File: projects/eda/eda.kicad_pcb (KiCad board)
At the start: 2 copper layers, 24.5 x 54.5 mm, 5 parts

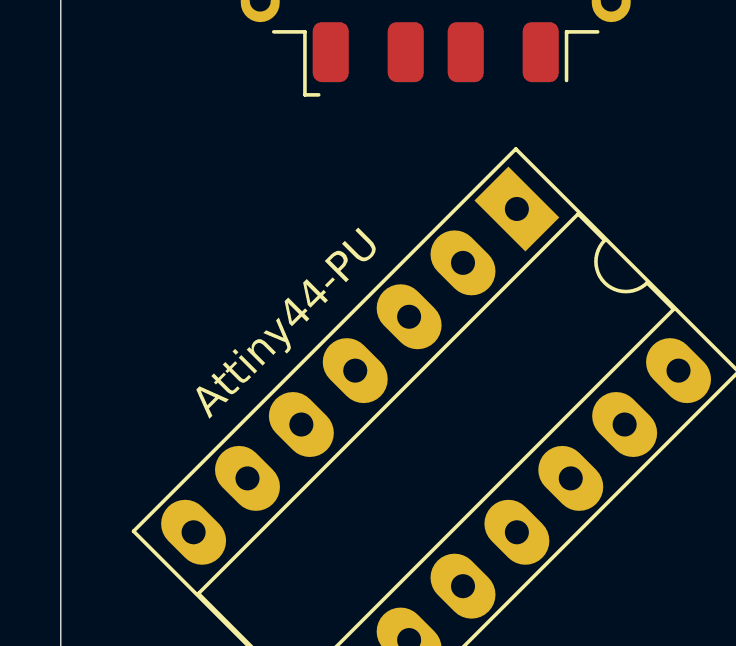
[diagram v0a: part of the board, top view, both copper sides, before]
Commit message: Add build scripts and update microcontroller. (#1)
* Port project to new microcontroller.

* Create make and build scripts.

* Update build script.

Updates the build script to use the new firmware target.

* Update PCB to reflect new microcontroller.
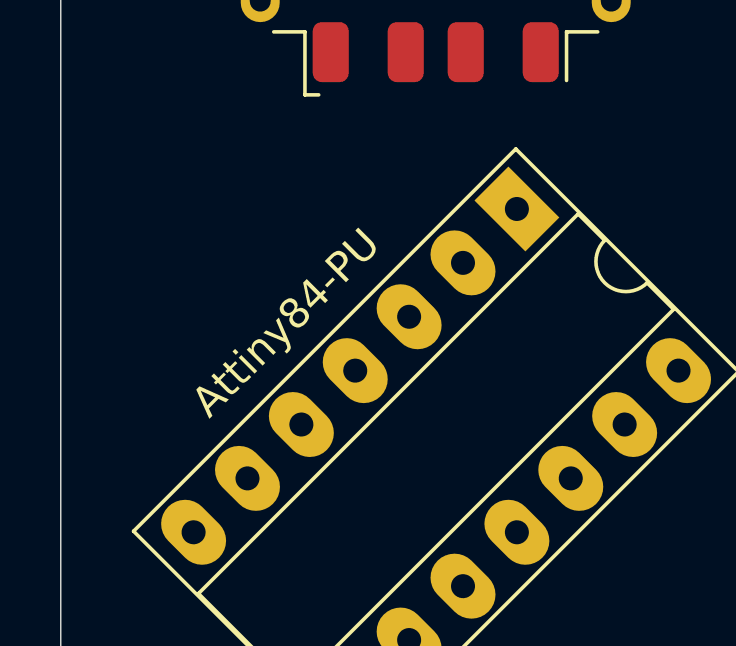
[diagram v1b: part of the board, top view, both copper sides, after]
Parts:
- renumbered Attiny44-PU to Attiny84-PU
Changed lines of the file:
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@@
 		(descr "14-lead though-hole mounted DIP package, row spacing 7.62 mm (300 mils), Socket, LongPads")
 		(tags "THT DIP DIL PDIP 2.54mm 7.62mm 300mil Socket LongPads")
-		(property "Reference" "Attiny44-PU"
-			(at -2.763821 8.132248 -135)
+		(property "Reference" "Attiny84-PU"
+			(at -2.763821 8.132248 225)
 			(layer "F.SilkS")
 			(effects
@@
 		(fp_arc
 			(start 4.810001 -1.33)
-			(mid 3.81 -0.33)
+			(mid 3.81 -0.330001)
 			(end 2.81 -1.33)
 			(stroke
@@
 		(tags "USB-A")
 		(property "Reference" "REF**"
-			(at 0 -7.5 270)
+			(at 0 -7.5 -90)
 			(layer "F.SilkS")
 			(hide yes)
@@
 		)
 		(property "Value" "USB_A_Molex_48037-2200_Horizontal"
-			(at 0 8 270)
+			(at 0 8 -90)
 			(layer "F.Fab")
 			(effects
@@
 		)
 		(fp_text user "${REFERENCE}"
-			(at 0 0 270)
-			(layer "F.Fab")
-			(effects
+			(at 0 0 -90)
+			(layer "F.Fab")
+			(effects

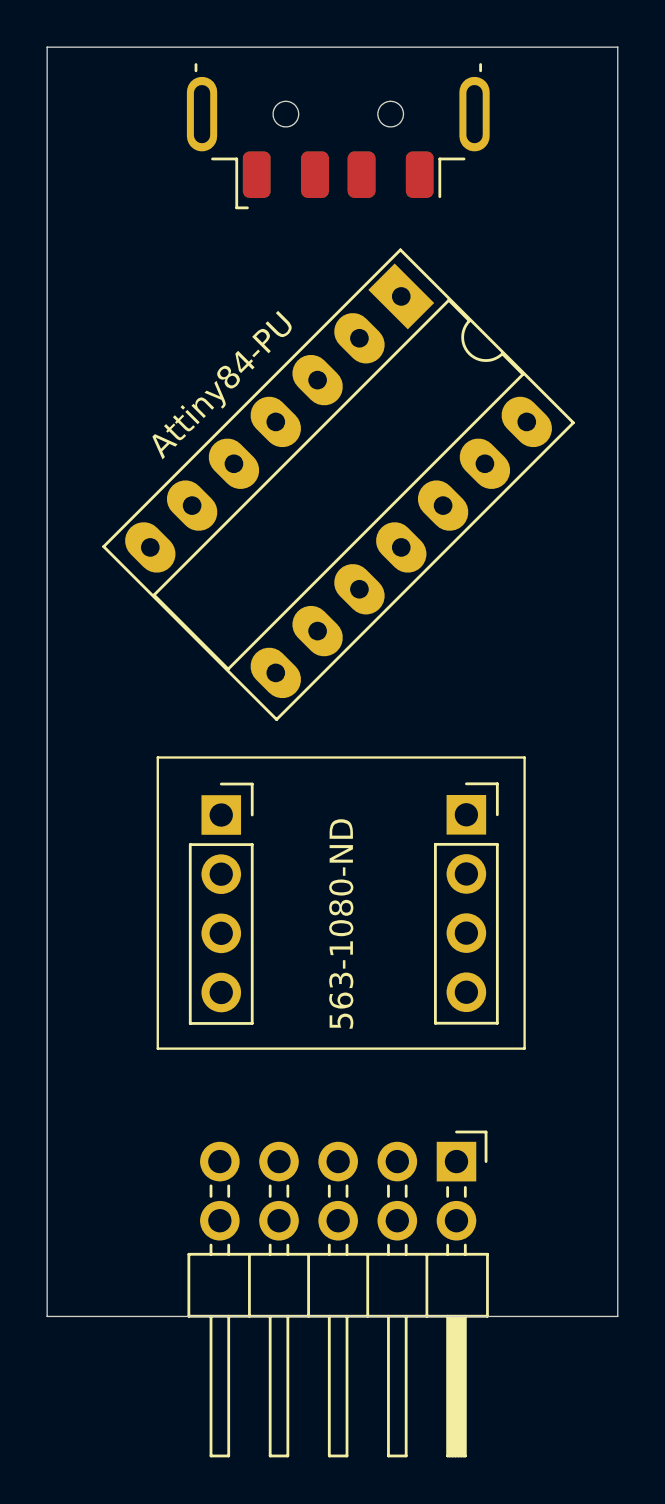
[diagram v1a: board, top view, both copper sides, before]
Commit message: Fix spacing of the 6 way switch.
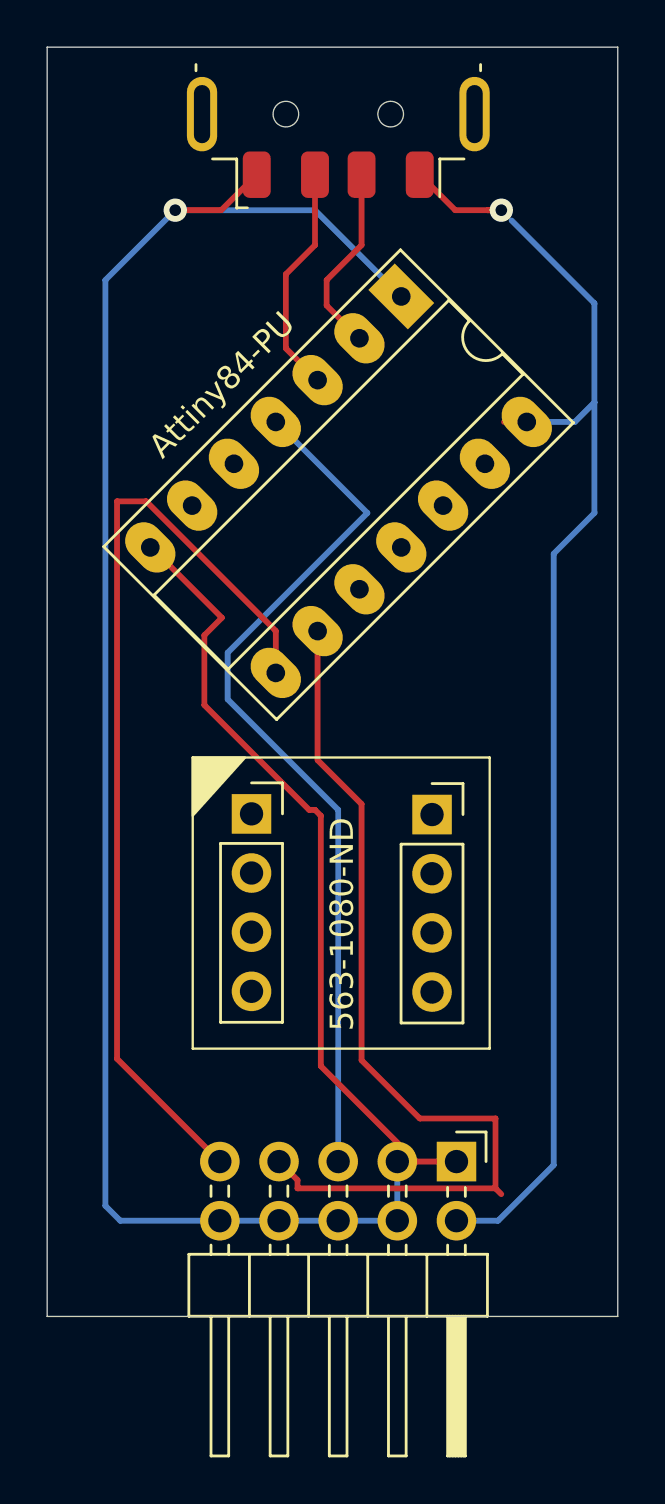
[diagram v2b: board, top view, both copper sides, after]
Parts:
- moved REF** 1.48 mm to (75.5, 95.5)
- moved REF** 1.30 mm to (67.8, 95.4)
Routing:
- net (no net): track 0.00 -> 301.6 mm, vias 0 -> 2
